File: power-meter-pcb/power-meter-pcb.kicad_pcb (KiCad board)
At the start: 4 copper layers, 29 x 55.5 mm, 72 parts, among them J1 Crank interconnect, J2 Debug, J3 USB4120-03-C_REVA, J4 Battery, J5 Side A, J6 Side B, Q1 AS2302, Q2 AS2302, Q3 AS2302, SW1 EN, SW2 BOOT, U1 ESP32-S3-WROOM-1, U2 P3T1755, U3 MCP73831-2-OT, U4 TPD3E001DRLR, U5 S-8261AAJMD-G2JT2U, U6 TPS63031DSK, U7 ADS1232IPW

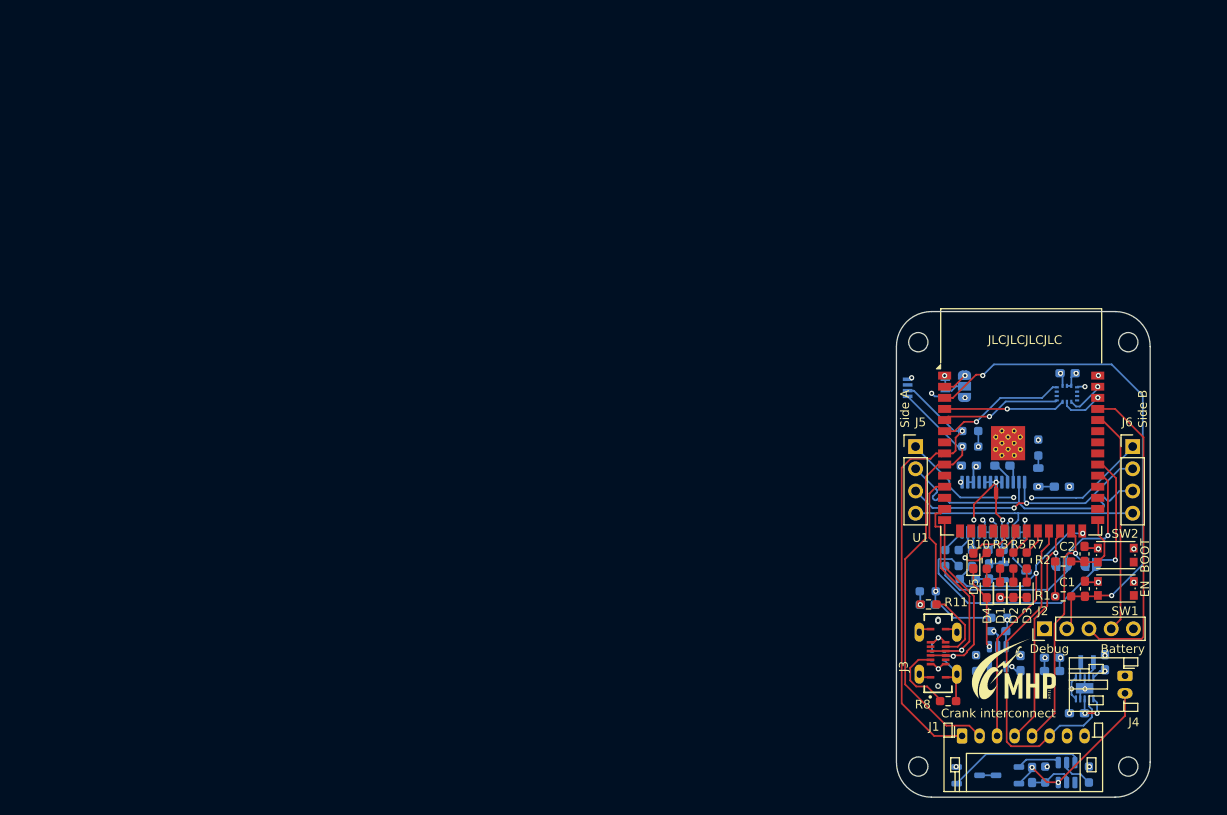
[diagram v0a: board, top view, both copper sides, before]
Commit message: Smaller PCB design started
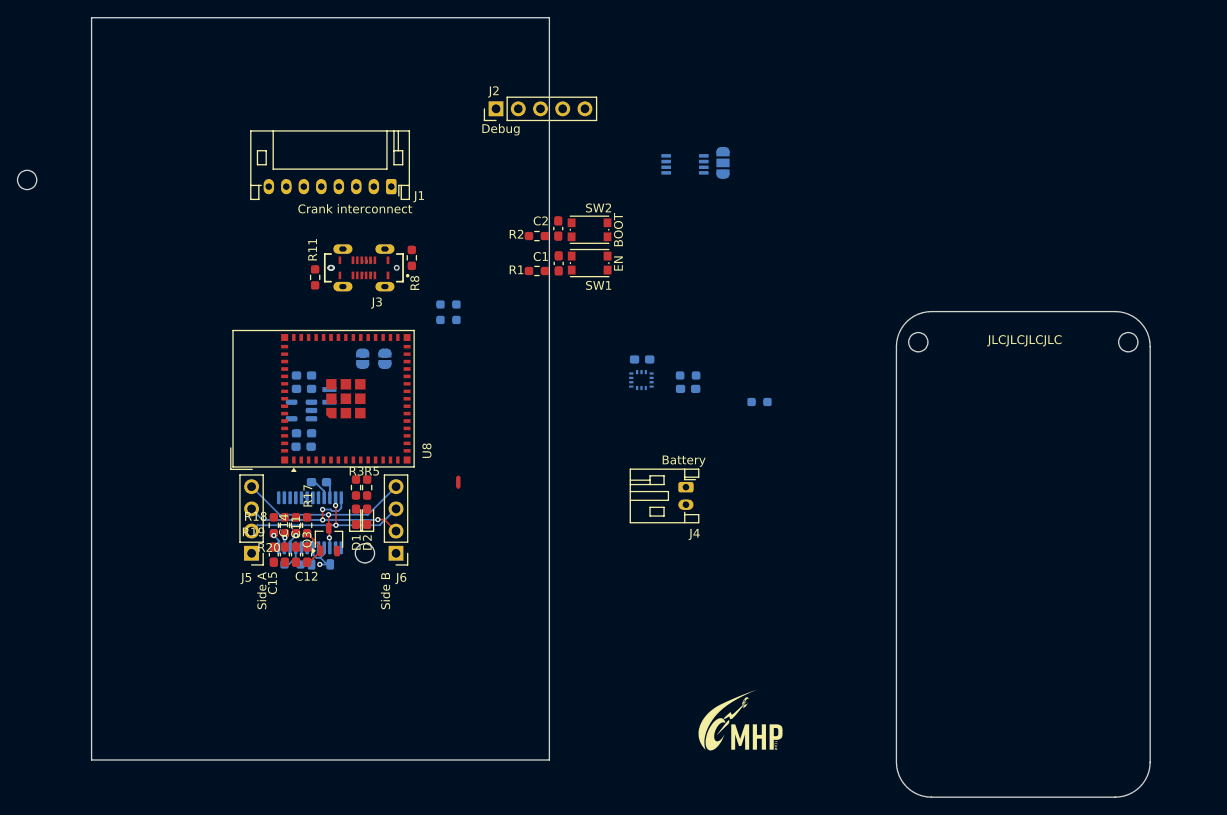
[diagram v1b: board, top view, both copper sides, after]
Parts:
- removed C3, C4: 10u, Capacitor_SMD:C_0603_1608Metric_Pad1.08x0.95mm_HandSolder
- removed C6: 0.1u, Capacitor_SMD:C_0603_1608Metric_Pad1.08x0.95mm_HandSolder
- removed D3, D4: LED, LED_SMD:LED_0603_1608Metric_Pad1.05x0.95mm_HandSolder
- removed D5: D, Diode_SMD:D_0603_1608Metric_Pad1.05x0.95mm_HandSolder
- removed Q1, Q2: AS2302, Package_TO_SOT_SMD:TSOT-23
- removed R10, R13: 470, Resistor_SMD:R_0603_1608Metric_Pad0.98x0.95mm_HandSolder
- removed R12: 2k, Resistor_SMD:R_0603_1608Metric_Pad0.98x0.95mm_HandSolder
- removed R7: 150, Resistor_SMD:R_0603_1608Metric_Pad0.98x0.95mm_HandSolder
- removed R9: 2.2k, Resistor_SMD:R_0603_1608Metric_Pad0.98x0.95mm_HandSolder
- removed U3: MCP73831-2-OT, Package_TO_SOT_SMD:SOT-23-5
- removed U5: S-8261AAJMD-G2JT2U, Package_TO_SOT_SMD:SOT-23-6
- removed U6: TPS63031DSK, Package_SON:WSON-10-1EP_2.5x2.5mm_P0.5mm_EP1.2x2mm
- added U8: ESP32-S3-MINI-1, RF_Module:ESP32-S2-MINI-1, F.Cu at (66.0, 76.6)
- C11, C12, C14, C15, Q3, R17, R18, R19, R20: moved to F.Cu
- U1: value ESP32-S3-WROOM-1 -> TPS613221ADBV; footprint RF_Module:ESP32-S3-WROOM-1 -> Package_TO_SOT_SMD:SOT-23-5; moved to B.Cu
- moved H3 142.6 mm to (32.2, 51.6)
- moved C5 97.2 mm to (63.8, 73.9), turned to 180 degrees
- moved C7 95.8 mm to (63.8, 75.5)
- moved L1 91.8 mm to (66.7, 76.3), turned to -90 degrees
- moved J1 90.5 mm to (73.8, 52.3), turned to 180 degrees
- moved C10 89.7 mm to (63.8, 80.5)
- moved C8 88.9 mm to (63.8, 82.1)
- moved C11 87.9 mm to (62.9, 94.4), turned to 90 degrees
- moved JP2 86.5 mm to (70.5, 72.0), turned to 90 degrees
- moved J2 86.4 mm to (85.8, 43.5)
- moved R16 86.3 mm to (62.5, 95.5), turned to 0 degrees
- moved J6 85.1 mm to (74.3, 94.2), turned to 180 degrees
- moved FB1 82.6 mm to (65.7, 95.5), turned to 0 degrees
- moved U1 82.3 mm to (63.5, 77.9), turned to 180 degrees
- moved C14 81.2 mm to (61.6, 94.4), turned to 90 degrees
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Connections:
- C7 pad 1: Net-(U6-EN) -> +BATT
- J4 pad 2: Net-(J4--) -> GNDD
- L1 pad 1: Net-(U6-L2) -> +BATT
- L1 pad 2: Net-(U6-L1) -> Net-(U1-SW)
- R17 pad 1: /AMP_PWDN -> /Power save
- U1 pad 1: GNDD -> Net-(U1-SW)
- U1 pad 2: +3.3V -> GNDD
- U1 pad 3: /EN -> unconnected-(U1-NC-Pad3)
- U1 pad 4: /Accelerometer/SPI.SDI -> +3.3V
- U1 pad 5: /Accelerometer/SPI.SDO -> unconnected-(U1-NC-Pad5)
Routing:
- net /EN: track 58.7 -> 0.00 mm, vias 2 -> 0
- net /I2C.SDA: track 53.6 -> 0.00 mm, vias 1 -> 0
- net /I2C.SCL: track 50.4 -> 0.00 mm, vias 1 -> 0
- net +3.3VA: track 48.3 -> 5.70 mm, vias 5 -> 1
- net /AMP_PWDN: track 40.2 -> 0.00 mm, vias 2 -> 0
- net /AMP1.SCLK: track 40.2 -> 0.00 mm, vias 1 -> 0
- net /Power save: track 39.7 -> 0.00 mm
- net GNDD: track 39.2 -> 0.00 mm, vias 23 -> 0
- net /UART.TX: track 36.2 -> 0.00 mm
- net /AMP1.DOUT: track 31.7 -> 0.00 mm, vias 1 -> 0
- net /AMP2.SCLK: track 27.9 -> 0.00 mm, vias 1 -> 0
- net /AMP2.DOUT: track 27.0 -> 0.00 mm, vias 1 -> 0
- net /UART.RX: track 25.7 -> 0.00 mm
- net /USB and power supply/USB.D_N: track 24.8 -> 0.00 mm, vias 1 -> 0
- net /USB and power supply/USB.D_P: track 22.9 -> 0.00 mm, vias 1 -> 0
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- removed copper zone on In1.Cu, net +3.3V
- removed copper zone on In1.Cu, net +5V
- removed copper zone on In1.Cu, net +BATT
- removed copper zone on In2.Cu, net GNDA
- removed copper zone on In2.Cu, net GNDD
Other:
- board size 29 x 55.5 mm -> 121 x 89.1 mm

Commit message: Smaller board layout planned
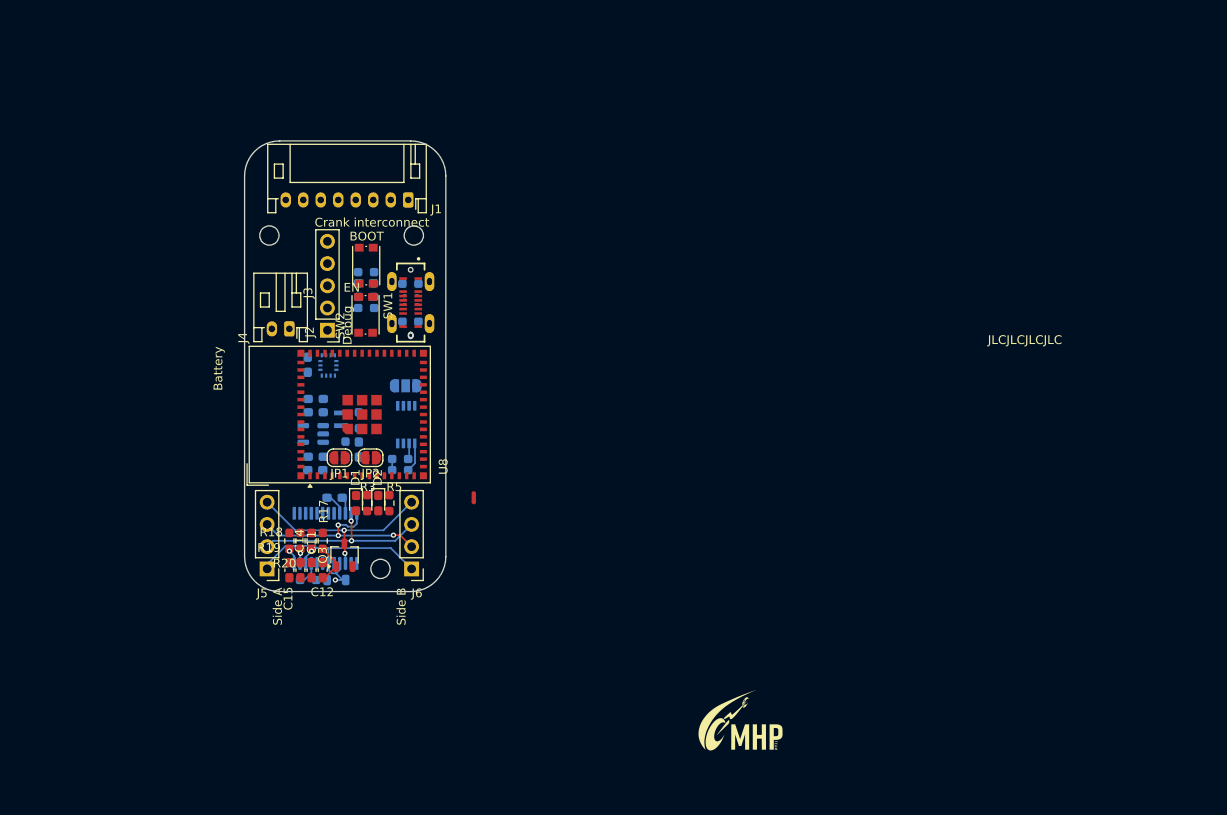
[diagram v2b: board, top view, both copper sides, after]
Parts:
- removed the H1 at (134.0, 70.1)
- C1, C2, R1, R11, R2, R8: moved to B.Cu
- JP1, JP2: moved to F.Cu
- moved H1 82.6 mm to (76.4, 57.9)
- moved J4 48.8 mm to (62.1, 68.6), turned to 180 degrees
- moved R14 45.8 mm to (70.1, 79.0), turned to -90 degrees
- moved JP3 44.3 mm to (75.4, 75.1), turned to 180 degrees
- moved U2 43.6 mm to (75.5, 79.5), turned to 90 degrees
- moved R15 40.1 mm to (68.6, 82.4), turned to -90 degrees
- moved C9 38.3 mm to (70.1, 82.4), turned to -90 degrees
- moved C16 38.2 mm to (64.2, 72.7), turned to 90 degrees
- moved MT1 35.8 mm to (66.6, 72.8), turned to 90 degrees
- moved J2 31.8 mm to (66.5, 68.8), turned to 180 degrees
- moved H2 28.4 mm to (59.9, 57.9)
- moved SW1 26.3 mm to (70.8, 67.0), turned to 90 degrees
- moved SW2 25.9 mm to (70.9, 61.4), turned to 90 degrees
- moved C2 22.8 mm to (70.9, 63.4), turned to 0 degrees
- moved C1 22.3 mm to (70.9, 64.9), turned to 0 degrees
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- renumbered H2 to H1, H3 to H2, H4 to H3
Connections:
- U8 pad 10: /Accelerometer/Interrupt -> /AMP_PWDN
- U8 pad 11: unconnected-(U8-IO7-Pad11) -> /Power save
- U8 pad 12: unconnected-(U8-IO8-Pad12) -> /LED1
- U8 pad 13: unconnected-(U8-IO9-Pad13) -> /LED2
- U8 pad 16: /LED1 -> unconnected-(U8-IO12-Pad16)
- U8 pad 17: /LED2 -> unconnected-(U8-IO13-Pad17)
- U8 pad 18: /LED3 -> unconnected-(U8-IO14-Pad18)
- U8 pad 19: /I2C.SDA -> unconnected-(U8-IO15-Pad19)
- U8 pad 20: /I2C.SCL -> unconnected-(U8-IO16-Pad20)
- U8 pad 25: /Power save -> unconnected-(U8-IO21-Pad25)
- U8 pad 27: /AMP2.DOUT -> unconnected-(U8-IO47-Pad27)
- U8 pad 30: /AMP2.SCLK -> unconnected-(U8-IO48-Pad30)
- U8 pad 34: /AMP1.DOUT -> unconnected-(U8-IO38-Pad34)
- U8 pad 35: /AMP1.SCLK -> unconnected-(U8-IO39-Pad35)
- U8 pad 41: /AMP_PWDN -> unconnected-(U8-IO45-Pad41)
- U8 pad 5: /Accelerometer/SPI.AC_CS -> /AMP1.DOUT
- U8 pad 6: /Accelerometer/SPI.SCLK -> /AMP2.DOUT
- U8 pad 8: /Accelerometer/SPI.SDI -> /AMP1.SCLK
- U8 pad 9: /Accelerometer/SPI.SDO -> /AMP2.SCLK
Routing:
- net +3.3VA: track 5.70 -> 26.5 mm
- net /I2C.SCL: track 0.00 -> 3.38 mm
- net /I2C.SDA: track 0.00 -> 1.82 mm
- net +3.3V: track 4.01 -> 5.28 mm
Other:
- board size 121 x 89.1 mm -> 23 x 51.5 mm

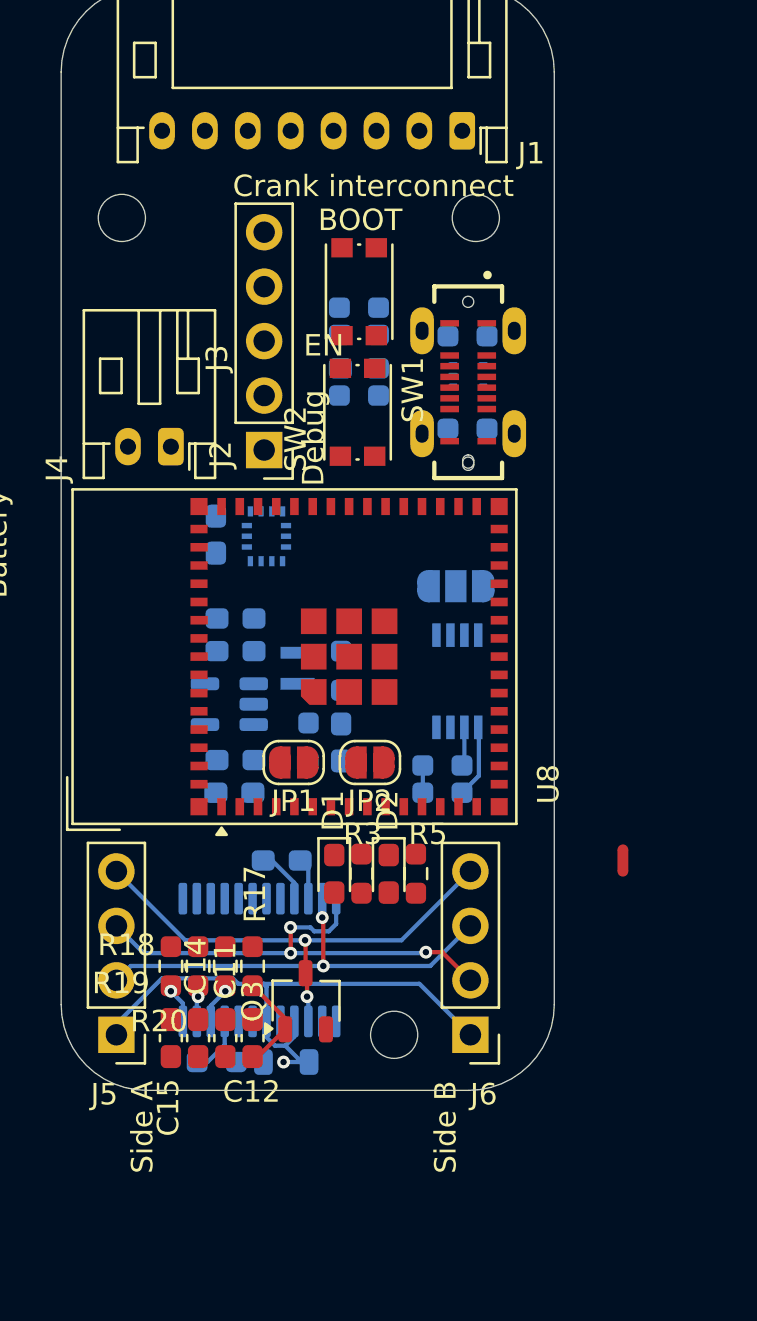
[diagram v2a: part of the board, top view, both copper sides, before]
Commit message: More track routing
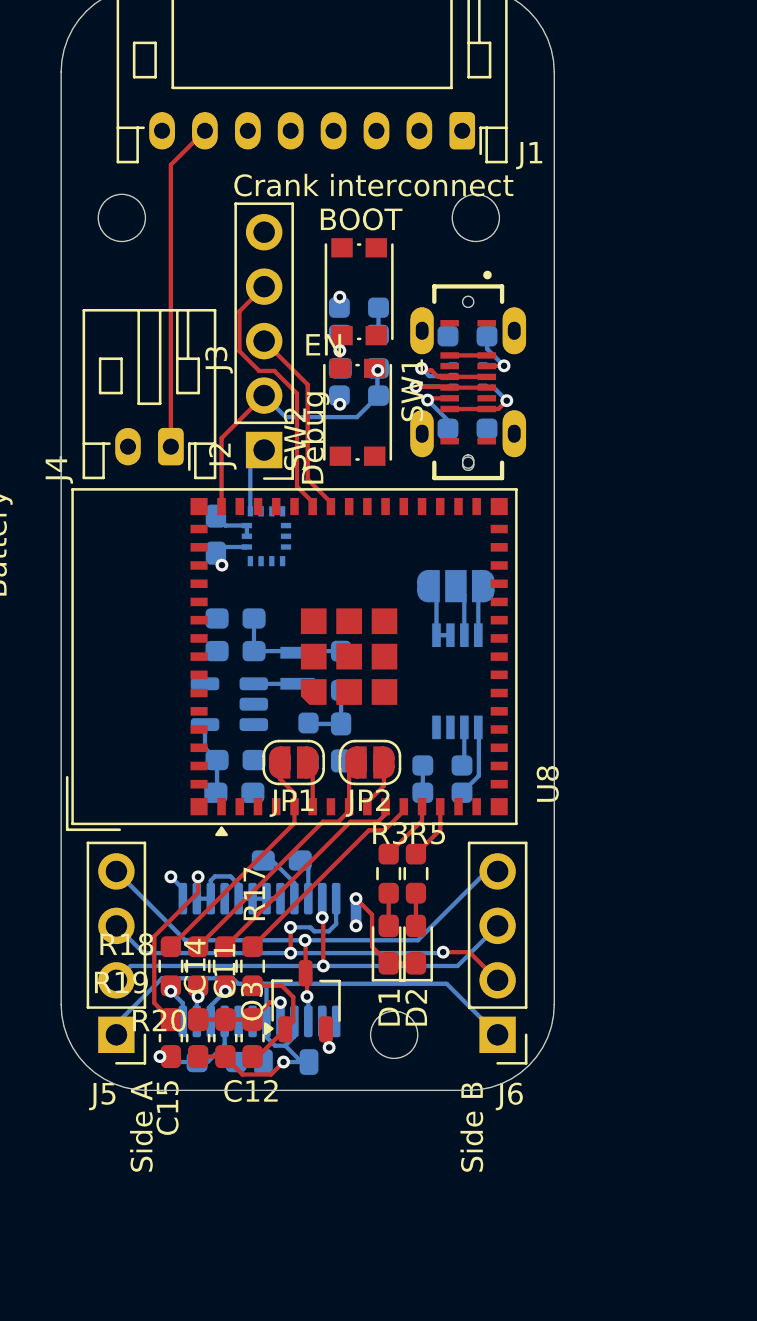
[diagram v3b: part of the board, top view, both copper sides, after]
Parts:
- NT2: moved to B.Cu
- moved NT2 12.7 mm to (70.8, 90.4)
- moved D1 4.17 mm to (72.3, 91.8), turned to 90 degrees
- moved D2 3.54 mm to (73.6, 91.8), turned to 90 degrees
- moved J6 1.27 mm to (77.4, 96.0)
- moved R3 1.27 mm to (72.3, 88.5)
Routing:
- net GNDD: track 0.00 -> 28.3 mm, vias 0 -> 3
- net +BATT: track 0.00 -> 21.0 mm
- net +3.3V: track 5.28 -> 20.1 mm, vias 0 -> 5
- net /EN: track 0.00 -> 13.5 mm, vias 0 -> 1
- net /UART.RX: track 0.00 -> 12.6 mm
- net /AMP1.SCLK: track 0.00 -> 12.1 mm
- net /AMP1.DOUT: track 0.00 -> 11.3 mm
- net /AMP_PWDN: track 0.00 -> 10.4 mm
- net /Power save: track 0.00 -> 9.87 mm
- net /UART.TX: track 0.00 -> 9.01 mm
- net GNDA: track 0.00 -> 7.96 mm, vias 0 -> 3
- net +3.3VA: track 26.5 -> 32.6 mm
- net +5V: track 0.00 -> 5.93 mm, vias 0 -> 1
- net /USB and power supply/USB.D_N: track 0.00 -> 5.05 mm, vias 0 -> 1
- net /USB and power supply/USB.D_P: track 0.00 -> 4.82 mm, vias 0 -> 1
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- added copper zone on In1.Cu, net +3.3V
- added copper zone on In2.Cu, net GNDA
- added copper zone on In2.Cu, net GNDD
